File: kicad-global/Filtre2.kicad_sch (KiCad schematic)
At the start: 48 parts, among them J10 Conn_JackBoard, J11 FilterCV2, J12 FilterOut2, J13 Conn_CircuitBoard, J14 Conn_JackBoard, J15 FilterIn2, J9 Conn_CircuitBoard, Q3 BC559, Q4 BC559, SW3 Hpass/Lpass Switch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

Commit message: fix issues and add guide
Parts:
- C15: value 10µF -> 10uF; Comment  (none) -> Electrolytic cap
- CUTCV2: Comment  (none) -> Use a small one (trimmer type)
- Q3, Q4: Comment  (none) -> Substitute BC558
- ResLv2: Comment  (none) -> variable resistor

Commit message: update worflow run condition + trimmer footprint update
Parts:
- ResLv2, ResVol2: footprint Potentiometer_THT:Potentiometer_Bourns_3386X_Horizontal -> Potentiometer_THT:Potentiometer_Bourns_3386C_Horizontal

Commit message: update value for trimmer
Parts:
- ResLv2: value 3.3k -> 10k
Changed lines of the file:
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@@
       (effects (font (size 1.27 1.27)) (justify right))
     )
-    (property "Value" "3.3k" (id 1) (at 193.04 96.52 90)
+    (property "Value" "10k" (id 1) (at 193.04 96.52 90)
       (effects (font (size 1.27 1.27)) (justify right))
     )

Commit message: update front panel and infos on components
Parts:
- CUTCV2: Comment  Use a small one (trimmer type) -> Use a small shaft (trimmer type)
- ResLv2: Comment  variable resistor -> Bourns 3386C
- ResVol2: Comment  (none) -> Bourns 3386C
- SW3: Comment  (none) -> DPDT Switch, On-Off-On

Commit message: update documentation + update repo layout
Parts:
- C15: Comment  Electrolytic cap -> (none)
- CUTCV2: footprint Synth:Pot-bourns-alpha -> Kicad-perso:Pot-bourns-alpha; Comment  Use a small shaft (trimmer type) -> (none)
- CUTOFF2, Res2: footprint Synth:Pot-bourns-alpha -> Kicad-perso:Pot-bourns-alpha
- J11, J12, J15: footprint Synth:Thonkiconn -> Kicad-perso:Thonkiconn
- Q3, Q4: Comment  Substitute BC558 -> (none); Comments (none) -> Substitute BC558
- ResLv2, ResVol2: Comment  Bourns 3386C -> (none); Comments (none) -> Use multi turn Cermet style 3296 pots
- SW3: footprint Synth:SW_DPDT_Toggle -> Kicad-perso:SW_DPDT_Toggle; Comment  DPDT Switch, On-Off-On -> (none); Comments (none) -> DPDT Switch, On-Off-On
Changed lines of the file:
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@@
       (effects (font (size 1.27 1.27)))
     )
-    (property "Footprint" "Synth:SW_DPDT_Toggle" (at 48.26 74.93 0)
-      (effects (font (size 1.27 1.27)) hide)
-    )
-    (property "Datasheet" "~" (at 48.26 74.93 0)
-      (effects (font (size 1.27 1.27)) hide)
-    )
-    (property "Comment " "DPDT Switch, On-Off-On " (at 48.26 80.01 0)
+    (property "Footprint" "Kicad-perso:SW_DPDT_Toggle" (at 48.26 74.93 0)
+      (effects (font (size 1.27 1.27)) hide)
+    )
+    (property "Datasheet" "https://www.taydaelectronics.com/mini-toggle-switch-1m-series-dpdt-on-on.html" (at 48.26 74.93 0)
+      (effects (font (size 1.27 1.27)) hide)
+    )
+    (property "Comments" "DPDT Switch, On-Off-On " (at 48.26 80.01 0)
       (effects (font (size 1.27 1.27)) hide)
     )
@@
       (effects (font (size 1.27 1.27)) hide)
     )
-    (property "Comment " "Electrolytic cap" (at 207.01 57.15 0)
-      (effects (font (size 1.27 1.27)) hide)
-    )
     (pin "1")
     (pin "2")
@@
       (effects (font (size 1.27 1.27)) (justify right))
     )
-    (property "Footprint" "Synth:Pot-bourns-alpha" (at 236.22 83.82 0)
+    (property "Footprint" "Kicad-perso:Pot-bourns-alpha" (at 236.22 83.82 0)
       (effects (font (size 1.27 1.27)) hide)
     )
@@
       (effects (font (size 1.27 1.27)) (justify right))
     )
-    (property "Footprint" "Synth:Pot-bourns-alpha" (at 182.88 148.59 0)
+    (property "Footprint" "Kicad-perso:Pot-bourns-alpha" (at 182.88 148.59 0)
       (effects (font (size 1.27 1.27)) hide)
     )
@@
       (effects (font (size 1.27 1.27)) (justify right))
     )
-    (property "Footprint" "Synth:Pot-bourns-alpha" (at 166.37 125.73 0)
+    (property "Footprint" "Kicad-perso:Pot-bourns-alpha" (at 166.37 125.73 0)
       (effects (font (size 1.27 1.27)) hide)
     )
     (property "Datasheet" "~" (at 166.37 125.73 0)
-      (effects (font (size 1.27 1.27)) hide)
-    )
-    (property "Comment " "Use a small shaft (trimmer type)" (at 166.37 125.73 0)
       (effects (font (size 1.27 1.27)) hide)
     )
@@
       (effects (font (size 1.27 1.27)) (justify left) hide)
     )
-    (property "Comment " "Substitute BC558" (at 101.6 116.84 0)
+    (property "Comments" "Substitute BC558" (at 101.6 116.84 0)
       (effects (font (size 1.27 1.27)) hide)
     )
@@
       (effects (font (size 1.27 1.27)) (justify left) hide)
     )
-    (property "Comment " "Substitute BC558" (at 120.65 116.84 0)
+    (property "Comments" "Substitute BC558" (at 120.65 116.84 0)
       (effects (font (size 1.27 1.27)) hide)
     )
@@
       (effects (font (size 1.27 1.27)) hide)
     )
-    (property "Datasheet" "~" (at 195.58 96.52 0)
-      (effects (font (size 1.27 1.27)) hide)
-    )
-    (property "Comment " "Bourns 3386C" (at 195.58 96.52 0)
+    (property "Datasheet" "https://www.taydaelectronics.com/potentiometer-variable-resistors/cermet-potentiometers/3296w/10k-ohm-trimmer-potentiometer-cermet-25-turns-3296w.html" (at 195.58 96.52 0)
+      (effects (font (size 1.27 1.27)) hide)
+    )
+    (property "Comments" "Use multi turn Cermet style 3296 pots " (at 195.58 96.52 0)
       (effects (font (size 1.27 1.27)) hide)
     )
@@
       (effects (font (size 1.27 1.27)) hide)
     )
-    (property "Datasheet" "~" (at 176.53 96.52 0)
-      (effects (font (size 1.27 1.27)) hide)
-    )
-    (property "Comment " "Bourns 3386C" (at 176.53 96.52 0)
+    (property "Datasheet" "https://www.taydaelectronics.com/potentiometer-variable-resistors/cermet-potentiometers/3296w/10k-ohm-trimmer-potentiometer-cermet-25-turns-3296w.html" (at 176.53 96.52 0)
+      (effects (font (size 1.27 1.27)) hide)
+    )
+    (property "Comments" "Use multi turn Cermet style 3296 pots " (at 176.53 96.52 0)
       (effects (font (size 1.27 1.27)) hide)
     )
@@
       (effects (font (size 1.27 1.27)))
     )
-    (property "Footprint" "Synth:Thonkiconn" (at 226.06 115.57 0)
+    (property "Footprint" "Kicad-perso:Thonkiconn" (at 226.06 115.57 0)
       (effects (font (size 1.27 1.27)) hide)
     )
@@
       (effects (font (size 1.27 1.27)))
     )
-    (property "Footprint" "Synth:Thonkiconn" (at 251.46 115.57 0)
+    (property "Footprint" "Kicad-perso:Thonkiconn" (at 251.46 115.57 0)
       (effects (font (size 1.27 1.27)) hide)
     )
@@
       (effects (font (size 1.27 1.27)))
     )
-    (property "Footprint" "Synth:Thonkiconn" (at 226.06 133.35 0)
-      (effects (font (size 1.27 1.27)) hide)
-    )
+    (property "Footprint" "Kicad-perso:Thonkiconn" (at 226.06 133.35 0)
+      (effects (font (size 1.27 1.27)) hide)
+    )

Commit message: update version number + hole size on front panel
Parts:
- CUTCV2: Comments (none) -> Use trimmer style pots for CUTCV1 and 2
- J11: value FilterCV2 -> Jack
- J12: value FilterOut2 -> Jack
- J15: value FilterIn2 -> Jack
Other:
- company: (none) -> Bleep Sound
- title: (none) -> MS20 VCF double
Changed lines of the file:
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@@
 (kicad_sch (version 20230121) (generator eeschema)
   (paper "A4")
+  (title_block
+    (title "MS20 VCF double")
+    (date "2023-10-06")
+    (rev "1.4")
+    (company "Bleep Sound")
+  )
   (junction (at 129.54 102.87) (diameter 0) (color 0 0 0 0)
   )
@@
       (effects (font (size 1.27 1.27)) hide)
     )
+    (property "Comments" "Use trimmer style pots for CUTCV1 and 2" (at 166.37 125.73 0)
+      (effects (font (size 1.27 1.27)) hide)
+    )
     (pin "1")
     (pin "2")
@@
       (effects (font (size 1.27 1.27)))
     )
-    (property "Value" "FilterCV2" (at 226.8728 112.1664 0)
+    (property "Value" "Jack" (at 226.8728 112.1664 0)
       (effects (font (size 1.27 1.27)))
     )
@@
       (effects (font (size 1.27 1.27)))
     )
-    (property "Value" "FilterOut2" (at 252.2728 112.1664 0)
+    (property "Value" "Jack" (at 252.2728 112.1664 0)
       (effects (font (size 1.27 1.27)))
     )
@@
       (effects (font (size 1.27 1.27)))
     )
-    (property "Value" "FilterIn2" (at 226.8728 129.9464 0)
-      (effects (font (size 1.27 1.27)))
-    )
+    (property "Value" "Jack" (at 226.8728 129.9464 0)
+      (effects (font (size 1.27 1.27)))
+    )

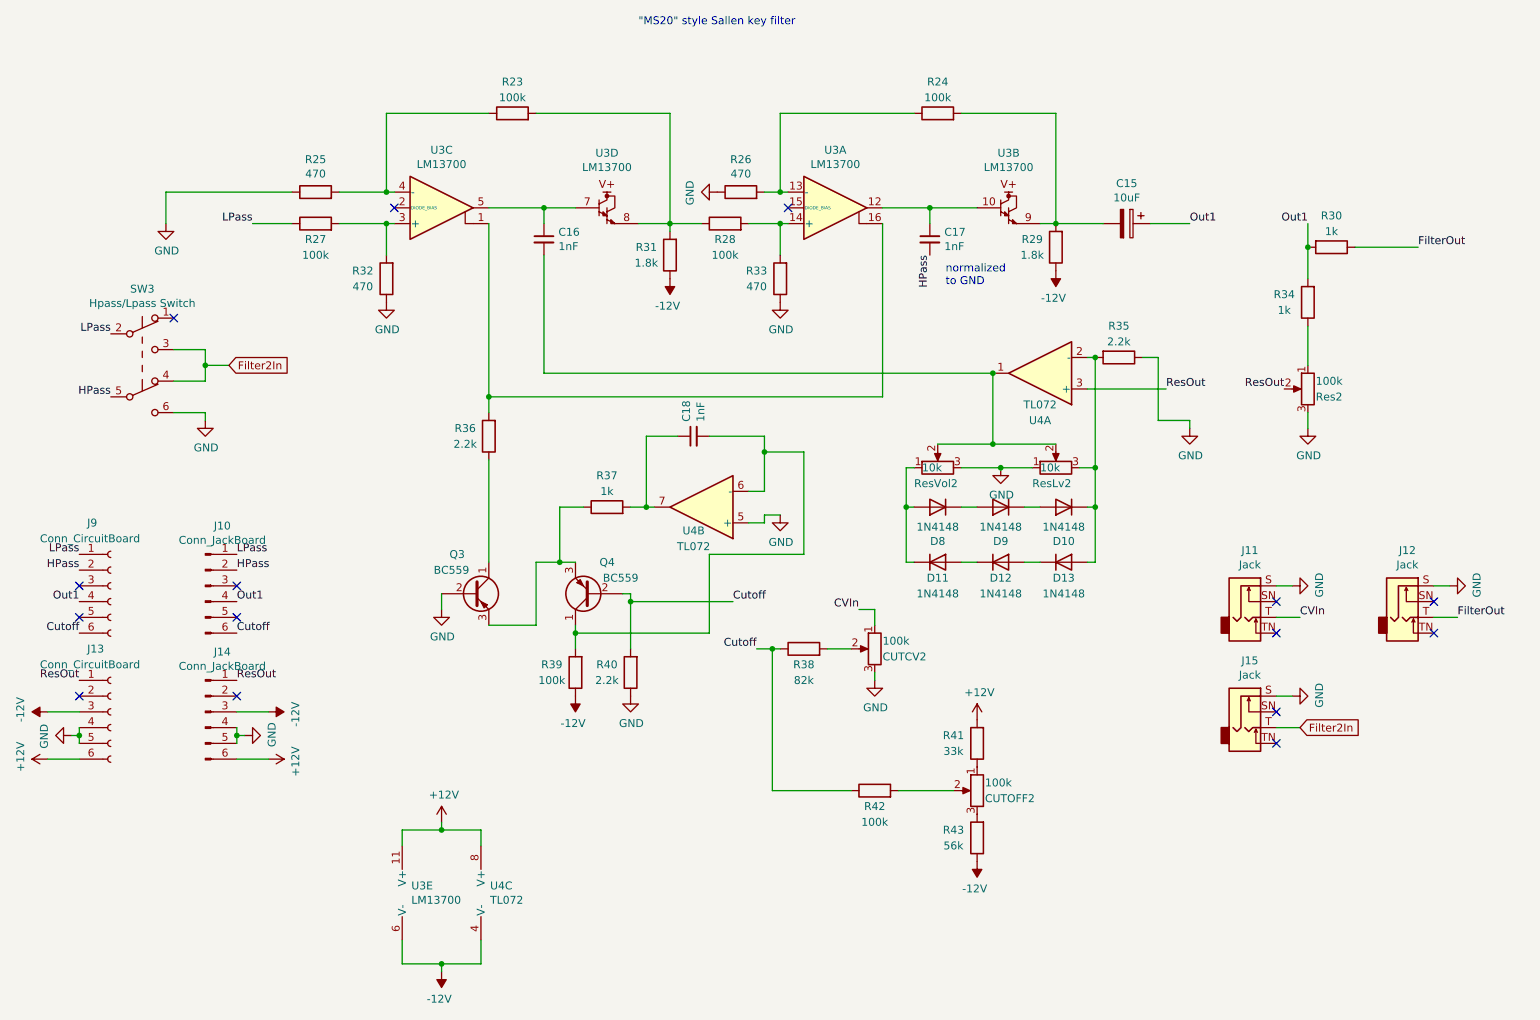
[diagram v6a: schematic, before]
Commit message: V2.0
new front panel layout
new normalisation for CV and in/out for bandpass filter
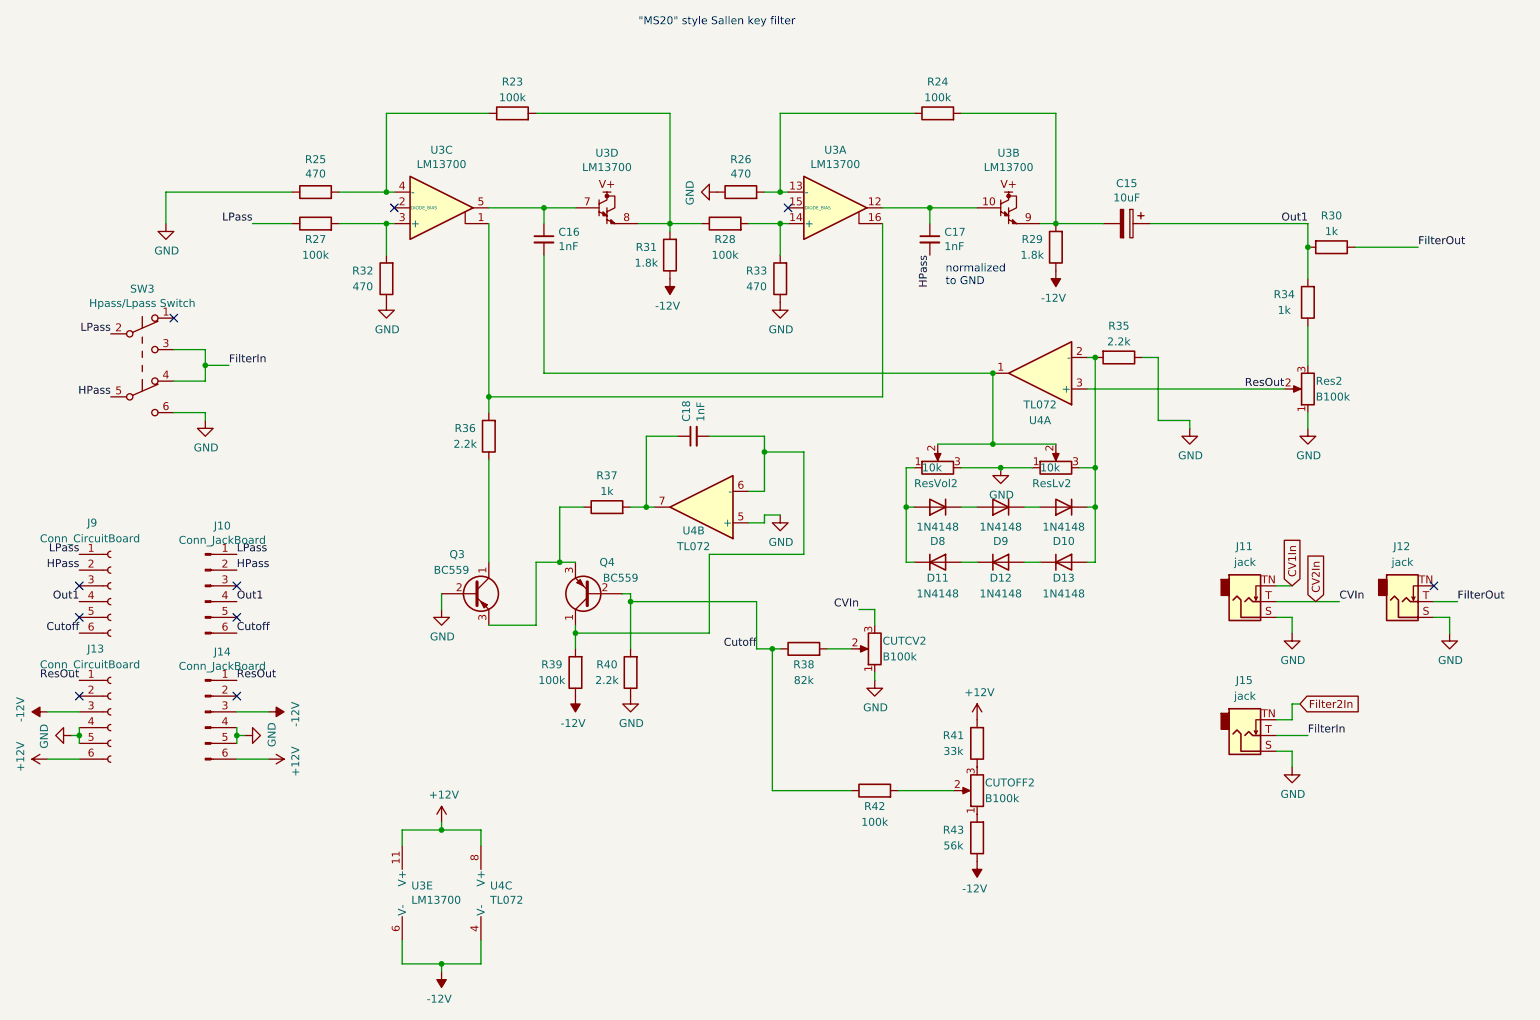
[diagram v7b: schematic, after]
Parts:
- removed J11, J12, J15: Jack, Kicad-perso:Thonkiconn, symbol Connector:AudioJack2_Switch
- added J11, J12, J15: jack, Kicad-perso:Thonkiconn, symbol Kicad-perso:AudioJack_Switch
- C15: Links (none) -> https://www.taydaelectronics.com/capacitors/electrolytic-ca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
- C16, C17, C18: Links (none) -> https://www.taydaelectronics.com/capacitors/monolithic-cera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
- CUTCV2, CUTOFF2, Res2: value 100k -> B100k; Links (none) -> https://www.thonk.co.uk/shop/alpha-9mm-pots/
- D10, D11, D12, D13, D8, D9: Links (none) -> https://www.taydaelectronics.com/1n4148-switching-signal-di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
- Q3, Q4: Links (none) -> https://www.taydaelectronics.com/bc558-bc558b-transistor-pn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
- R23, R24, R25, R26, R27, R28, R29, R30, R31, R32, R33, R34, R35, R36, R37, R38, R39, R40, R41, R42, R43: Links (none) -> https://www.taydaelectronics.com/resistors/1-4w-metal-film-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
- ResLv2, ResVol2: footprint Potentiometer_THT:Potentiometer_Bourns_3386C_Horizontal -> Potentiometer_THT:Potentiometer_Bourns_3296W_Vertical; Links (none) -> https://www.thonk.co.uk/shop/25-turn-trimmer-potentiometer/
- SW3: Links (none) -> https://www.taydaelectronics.com/mini-toggle-switch-dpdt-on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
- U3: Links (none) -> https://eu.mouser.com/c/semiconductors/amplifier-ics/transc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
- U4: Links (none) -> https://eu.mouser.com/ProductDetail/Texas-Instruments/TL072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
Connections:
- net CVIn is gone; now on net GND: CUTCV2.1
- net Filter2In: now also J15.TN; no longer SW3.3 (C), SW3.4 (A)
- net FilterOut: now also J12.T
- net GND: now also Res2.1, J11.S, J12.S, J15.S; no longer CUTCV2.3, Res2.3
- net at R34.1: now also Res2.3; no longer Res2.1
- net at CUTOFF2.1: now also R43.2; no longer R41.1
- net at CUTOFF2.3: now also R41.1; no longer R43.2
- new net CV1In: J11.TN
- new net CV2In: CUTCV2.3, J11.T
- new net FilterIn: J15.T, SW3.3 (C), SW3.4 (A)
- no-connect marks 15 -> 10
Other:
- moved on the sheet: CUTCV2, CUTOFF2, Res2
